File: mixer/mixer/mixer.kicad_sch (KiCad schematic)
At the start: 39 parts, among them J1 Power Connector, J10 Output, J11 Inverted, J2 Input 1, J3 Input 2, J4 Input 3, J5 Input 4, J6 Front_Board_Con, J7 Front_Board_Balance, J8 Back_Board_Conn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

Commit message: Updated mixer and multiple to use new common libs
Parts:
- RV1, RV2, RV3, RV4: footprint SamacSys_Parts:RD901F4015R1B100K00DL1 -> Alpha_Pots:Potentiometer_Alpha_RV09AF-40-20K_Single_Vertical
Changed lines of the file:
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@@
     (property "Reference" "RV1" (id 0) (at 71.12 35.56 90))
     (property "Value" "R_Potentiometer" (id 1) (at 71.12 38.1 90))
-    (property "Footprint" "SamacSys_Parts:RD901F4015R1B100K00DL1" (id 2) (at 71.12 31.75 0)
+    (property "Footprint" "Alpha_Pots:Potentiometer_Alpha_RV09AF-40-20K_Single_Vertical" (id 2) (at 71.12 31.75 0)
       (effects (font (size 1.27 1.27)) hide)
     )
@@
     (property "Reference" "RV4" (id 0) (at 71.12 128.27 90))
     (property "Value" "R_Potentiometer" (id 1) (at 71.12 130.81 90))
-    (property "Footprint" "SamacSys_Parts:RD901F4015R1B100K00DL1" (id 2) (at 71.12 124.46 0)
+    (property "Footprint" "Alpha_Pots:Potentiometer_Alpha_RV09AF-40-20K_Single_Vertical" (id 2) (at 71.12 124.46 0)
       (effects (font (size 1.27 1.27)) hide)
     )
@@
     (property "Reference" "RV3" (id 0) (at 71.12 96.52 90))
     (property "Value" "R_Potentiometer" (id 1) (at 71.12 99.06 90))
-    (property "Footprint" "SamacSys_Parts:RD901F4015R1B100K00DL1" (id 2) (at 71.12 92.71 0)
+    (property "Footprint" "Alpha_Pots:Potentiometer_Alpha_RV09AF-40-20K_Single_Vertical" (id 2) (at 71.12 92.71 0)
       (effects (font (size 1.27 1.27)) hide)
     )
@@
     (property "Reference" "RV2" (id 0) (at 71.12 64.77 90))
     (property "Value" "R_Potentiometer" (id 1) (at 71.12 67.31 90))
-    (property "Footprint" "SamacSys_Parts:RD901F4015R1B100K00DL1" (id 2) (at 71.12 60.96 0)
+    (property "Footprint" "Alpha_Pots:Potentiometer_Alpha_RV09AF-40-20K_Single_Vertical" (id 2) (at 71.12 60.96 0)
       (effects (font (size 1.27 1.27)) hide)
     )
@@
     )
     (path "/526d88b4-df89-426d-9d43-7c4891272783"
-      (reference "RV1") (unit 1) (value "R_Potentiometer") (footprint "SamacSys_Parts:RD901F4015R1B100K00DL1")
+      (reference "RV1") (unit 1) (value "R_Potentiometer") (footprint "Alpha_Pots:Potentiometer_Alpha_RV09AF-40-20K_Single_Vertical")
     )
     (path "/c4f786f9-d011-4942-b093-6c017cd0bddc"
-      (reference "RV2") (unit 1) (value "R_Potentiometer") (footprint "SamacSys_Parts:RD901F4015R1B100K00DL1")
+      (reference "RV2") (unit 1) (value "R_Potentiometer") (footprint "Alpha_Pots:Potentiometer_Alpha_RV09AF-40-20K_Single_Vertical")
     )
     (path "/a3d45bfe-07de-40cb-b2a5-932eb2c3ca54"
-      (reference "RV3") (unit 1) (value "R_Potentiometer") (footprint "SamacSys_Parts:RD901F4015R1B100K00DL1")
+      (reference "RV3") (unit 1) (value "R_Potentiometer") (footprint "Alpha_Pots:Potentiometer_Alpha_RV09AF-40-20K_Single_Vertical")
     )
     (path "/819be6ca-b719-48a6-abd2-55a66f6239ae"
-      (reference "RV4") (unit 1) (value "R_Potentiometer") (footprint "SamacSys_Parts:RD901F4015R1B100K00DL1")
+      (reference "RV4") (unit 1) (value "R_Potentiometer") (footprint "Alpha_Pots:Potentiometer_Alpha_RV09AF-40-20K_Single_Vertical")
     )
     (path "/84bc8567-aca5-4add-a475-a609af2ece64"

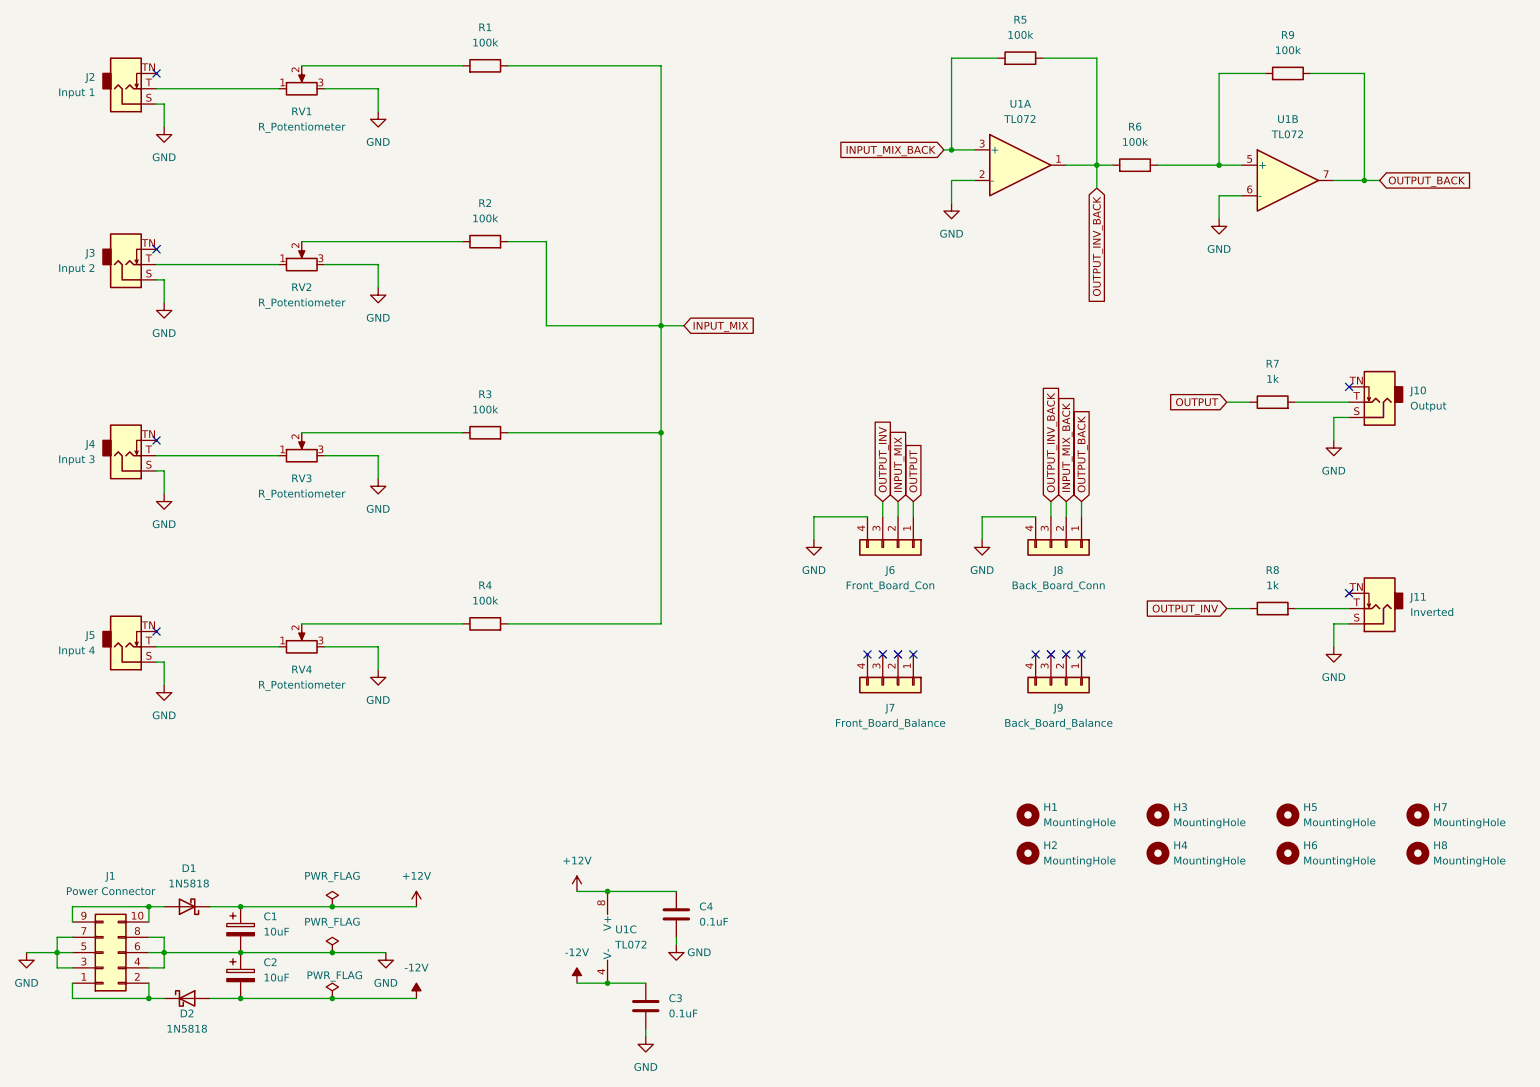
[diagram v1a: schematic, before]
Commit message: Added rev2 of mixer. Fixed opamp configuation and panel connector layout
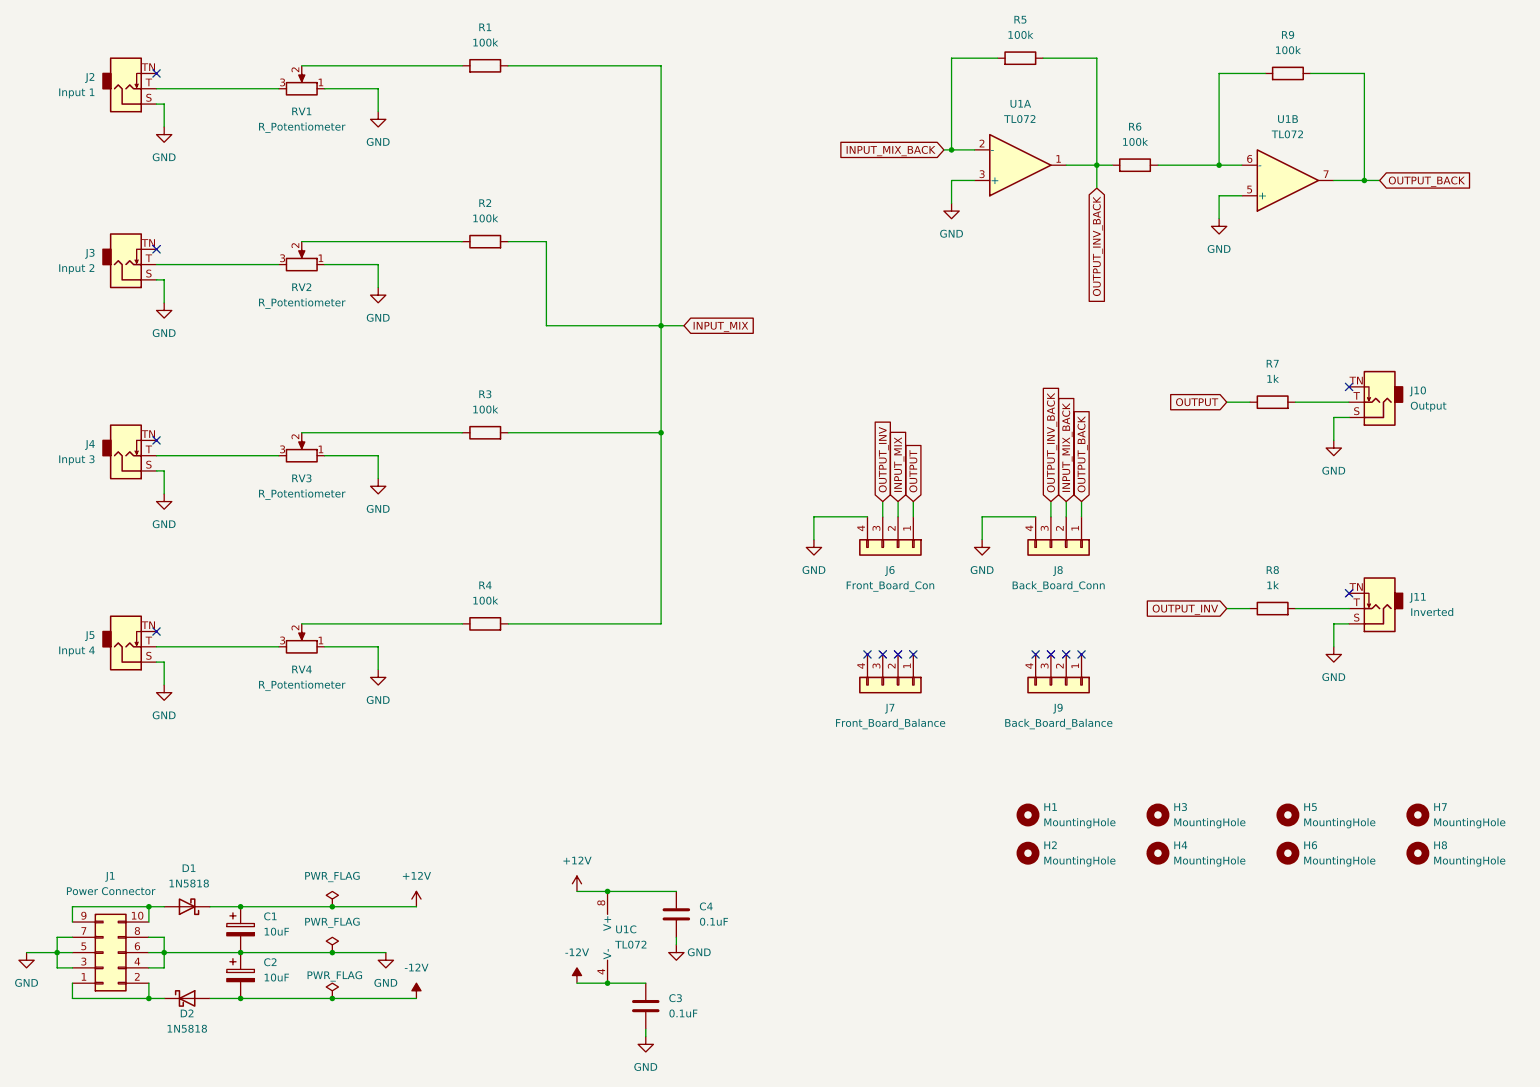
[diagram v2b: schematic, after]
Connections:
- net GND: now also RV1.1, RV2.1, RV3.1, RV4.1, U1.3 (+), U1.5 (+); no longer RV1.3, RV2.3, RV3.3, RV4.3, U1.2 (-), U1.6 (-)
- net INPUT_MIX_BACK: now also U1.2 (-); no longer U1.3 (+)
- net at R6.1, R9.2: now also U1.6 (-); no longer U1.5 (+)
- net at J3.T: now also RV2.3; no longer RV2.1
- net at J2.T: now also RV1.3; no longer RV1.1
- net at J5.T: now also RV4.3; no longer RV4.1
- net at J4.T: now also RV3.3; no longer RV3.1
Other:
- moved on the sheet: RV1, RV2, RV3, RV4
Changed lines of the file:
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@@
   (title_block
     (title "Simple Mixer")
-    (rev "1")
+    (rev "2")
     (company "Northridge Devices")
   )
@@
     (pin "2")
   )
-  (symbol (lib_id "Device:R_Potentiometer") (at 71.12 31.75 90) (unit 1)
+  (symbol (lib_id "Device:R_Potentiometer") (at 71.12 31.75 270) (mirror x) (unit 1)
     (in_bom yes) (on_board yes) (fields_autoplaced)
     (property "Reference" "RV1" (id 0) (at 71.12 35.56 90))
@@
     )
   )
-  (symbol (lib_id "Amplifier_Operational:TL072") (at 234.95 46.99 0) (unit 2)
+  (symbol (lib_id "Amplifier_Operational:TL072") (at 234.95 46.99 0) (mirror x) (unit 2)
     (in_bom yes) (on_board yes) (fields_autoplaced)
     (property "Reference" "U1" (id 0) (at 234.95 36.83 0))
@@
     (pin "1")
   )
-  (symbol (lib_id "Device:R_Potentiometer") (at 71.12 124.46 90) (unit 1)
+  (symbol (lib_id "Device:R_Potentiometer") (at 71.12 124.46 270) (mirror x) (unit 1)
     (in_bom yes) (on_board yes) (fields_autoplaced)
     (property "Reference" "RV4" (id 0) (at 71.12 128.27 90))
@@
     (pin "3")
   )
-  (symbol (lib_id "Amplifier_Operational:TL072") (at 190.5 44.45 0) (unit 1)
+  (symbol (lib_id "Amplifier_Operational:TL072") (at 190.5 44.45 0) (mirror x) (unit 1)
     (in_bom yes) (on_board yes) (fields_autoplaced)
     (property "Reference" "U1" (id 0) (at 190.5 34.29 0))
@@
     (pin "1")
   )
-  (symbol (lib_id "Device:R_Potentiometer") (at 71.12 92.71 90) (unit 1)
+  (symbol (lib_id "Device:R_Potentiometer") (at 71.12 92.71 270) (mirror x) (unit 1)
     (in_bom yes) (on_board yes) (fields_autoplaced)
     (property "Reference" "RV3" (id 0) (at 71.12 96.52 90))
@@
     (pin "9")
   )
-  (symbol (lib_id "Device:R_Potentiometer") (at 71.12 60.96 90) (unit 1)
+  (symbol (lib_id "Device:R_Potentiometer") (at 71.12 60.96 270) (mirror x) (unit 1)
     (in_bom yes) (on_board yes) (fields_autoplaced)
     (property "Reference" "RV2" (id 0) (at 71.12 64.77 90))
